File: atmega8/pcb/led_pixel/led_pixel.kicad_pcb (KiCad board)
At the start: 2 copper layers, 50 x 50 mm, 68 parts, among them IC1 ATMEGA8-AI, P1 USB_OTG, P10 CONN_01X04, P2 RESET, P3 CONN_01X03, P4 MOSI, P5 MISO, P6 SCK, P7 CONN_01X03, P8 5V, P9 GND, U1 MC78M05CDT, U2 PT4115, U3 PT4115, U4 SN75176, U5 PT4115, Y1 CRYSTAL

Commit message: layout in process... :|
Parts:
- removed the C7 at (162.0, 72.0)
- removed JP2: DMX_ADR_0, proz_jumper:solderjumper
- removed JP3: DMX_ADR_1, proz_jumper:solderjumper
- removed JP4: DMX_ADR_2, proz_jumper:solderjumper
- removed JP5: DMX_ADR_3, proz_jumper:solderjumper
- removed JP6: DMX_ADR_4, proz_jumper:solderjumper
- removed JP7: DMX_ADR_5, proz_jumper:solderjumper
- removed JP8: DMX_ADR_6, proz_jumper:solderjumper
- removed JP9: DMX_ADR_7, proz_jumper:solderjumper
- removed the P4 at (138.4, 82.5)
- removed the P5 at (141.0, 82.5)
- removed P6: SCK, Socket_Strips:Socket_Strip_Straight_1x01
- removed P8: 5V, Socket_Strips:Socket_Strip_Straight_1x01
- removed P9: GND, Socket_Strips:Socket_Strip_Straight_1x01
- added SW1: SW_DIP_x08, proz_switch:SW_DIP_x8_SMD_2.54, F.Cu at (168.3, 81.9)
- P2: value RESET -> ISP; footprint Socket_Strips:Socket_Strip_Straight_1x01 -> Connectors:IDC_Header_Straight_6pins
- moved P2 50.0 mm to (164.7, 41.7), turned to 270 degrees
- moved C10 14.4 mm to (137.3, 79.3)
- moved C3 13.2 mm to (148.0, 83.9), turned to 180 degrees
- moved P5 12.8 mm to (172.9, 111.8)
- moved C13 12.7 mm to (170.1, 104.0), turned to 270 degrees
- moved R16 12.7 mm to (168.8, 107.3)
- moved P3 12.4 mm to (172.9, 95.1)
- moved R15 11.6 mm to (168.8, 109.3), turned to 180 degrees
- moved C12 11.3 mm to (144.4, 111.8), turned to 180 degrees
- moved C14 11.3 mm to (132.7, 111.8), turned to 180 degrees
- moved C11 10.9 mm to (156.6, 111.8), turned to 180 degrees
- moved D7 9.96 mm to (164.2, 112.9), turned to 0 degrees
- moved R10 9.78 mm to (152.0, 110.8), turned to 270 degrees
- moved R12 9.71 mm to (140.3, 110.8), turned to 270 degrees
- moved R14 9.64 mm to (128.7, 110.8), turned to 270 degrees
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- renumbered C11 to C10, C12 to C11, C13 to C12, C14 to C13, C15 to C14, C8 to C7, C9 to C8, C10 to C9, D6 to D5, D5 to D6, P7 to P4, P10 to P5
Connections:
- net Net-(IC1-Pad28) renamed /DMX_5
- C4 pad 1: Net-(C4-Pad1) -> /RESET
- IC1 pad 17: Net-(IC1-Pad17) -> /SCK
- IC1 pad 2: Net-(IC1-Pad2) -> /DMX_6
- IC1 pad 23: Net-(IC1-Pad23) -> /DMX_0
- IC1 pad 24: Net-(IC1-Pad24) -> /DMX_1
- IC1 pad 25: Net-(IC1-Pad25) -> /DMX_2
- IC1 pad 26: Net-(IC1-Pad26) -> /DMX_3
- IC1 pad 27: Net-(IC1-Pad27) -> /DMX_4
- IC1 pad 29: Net-(C4-Pad1) -> /RESET
- IC1 pad 9: Net-(IC1-Pad9) -> /DMX_7
- P2 pad 1: Net-(C4-Pad1) -> /LED_B
- R4 pad 2: Net-(C4-Pad1) -> /RESET
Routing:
- net /DMX_5: track 36.4 -> 0.00 mm, vias 1 -> 0
- net +5V: track 38.4 -> 2.10 mm
- net /LED_R_A: track 3.60 -> 36.1 mm, vias 0 -> 4
- net /LED_B_A: track 0.00 -> 29.6 mm
- net Net-(IC1-Pad19): track 25.1 -> 0.00 mm, vias 1 -> 0
- net GND: track 45.4 -> 21.1 mm, vias 4 -> 1
- net /LED_B_K: track 0.00 -> 24.2 mm
- net /LED_G_A: track 0.00 -> 22.9 mm, vias 0 -> 2
- net /DMX_TX: track 21.3 -> 0.00 mm, vias 2 -> 0
- net /DMX_DIR: track 21.1 -> 0.00 mm, vias 2 -> 0
- net /LED_G_K: track 0.00 -> 18.8 mm
- net /LED_R: track 20.2 -> 2.68 mm, vias 2 -> 0
- net Net-(IC1-Pad9): track 17.3 -> 0.00 mm, vias 2 -> 0
- net /UDB_+: track 16.3 -> 0.00 mm
- net Net-(C4-Pad1): track 14.9 -> 0.00 mm, vias 2 -> 0
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
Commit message: finished first shot of the layout...
there are mounting holes missing...
...so what ;)
I hope to find a place for them this week...
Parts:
- added G***: LOGO, proz_logo:Shimatta_SolderMask, B.Cu at (136.0, 111.6)
- added REF**: MountingHole_3.2mm_M3_DIN965, Mounting_Holes:MountingHole_3.2mm_M3_DIN965, F.Cu at (111.9, 83.7)
- added REF**: KiCAD Logo, Symbols:Symbol_KiCAD-Logo_CopperAndSilkScreenTop, B.Cu at (166.5, 82.4)
- added REF***: OSHW-Logo2_7.3x6mm_Copper, Symbols:OSHW-Logo2_7.3x6mm_Copper, B.Cu at (169.1, 90.0)
- added REF***: WEEE-Logo_4.2x6mm_SilkScreen, Symbols:WEEE-Logo_4.2x6mm_SilkScreen, B.Cu at (167.8, 110.3)
- P2: moved to B.Cu
- moved P2 49.6 mm to (137.3, 83.0), turned to 0 degrees
- moved R16 2.59 mm to (166.3, 106.8)
- moved R15 2.54 mm to (166.3, 109.3)
- moved C13 0.80 mm to (169.3, 104.2)
- moved C5 0.77 mm to (155.8, 85.2)
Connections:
- P3 pad 2: Net-(IC1-Pad19) -> Net-(IC1-Pad22)
- P3 pad 3: Net-(IC1-Pad22) -> Net-(IC1-Pad19)
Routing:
- net GND: track 21.1 -> 202.9 mm, vias 1 -> 186
- net +5V: track 2.10 -> 158.3 mm, vias 0 -> 6
- net /LED_B: track 0.00 -> 46.7 mm, vias 0 -> 2
- net /DMX_DIR: track 0.00 -> 37.2 mm, vias 0 -> 2
- net /LED_G: track 0.00 -> 37.0 mm, vias 0 -> 3
- net /LED_R: track 2.68 -> 39.6 mm, vias 0 -> 4
- net Net-(IC1-Pad19): track 0.00 -> 33.1 mm
- net /DMX_5: track 0.00 -> 32.7 mm
- net /DMX_RX: track 0.00 -> 29.1 mm
- net VCC: track 19.5 -> 47.8 mm
- net Net-(IC1-Pad22): track 0.00 -> 28.2 mm
- net /RESET: track 0.00 -> 25.5 mm, vias 0 -> 3
- net /DMX_TX: track 0.00 -> 24.8 mm, vias 0 -> 2
- net /Bootloader: track 0.00 -> 19.3 mm
- net /DMX_6: track 0.00 -> 16.6 mm
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- added copper zone on B.Cu, net GND
- added copper zone on F.Cu, net GND
- added copper zone on F.Cu, net VCC

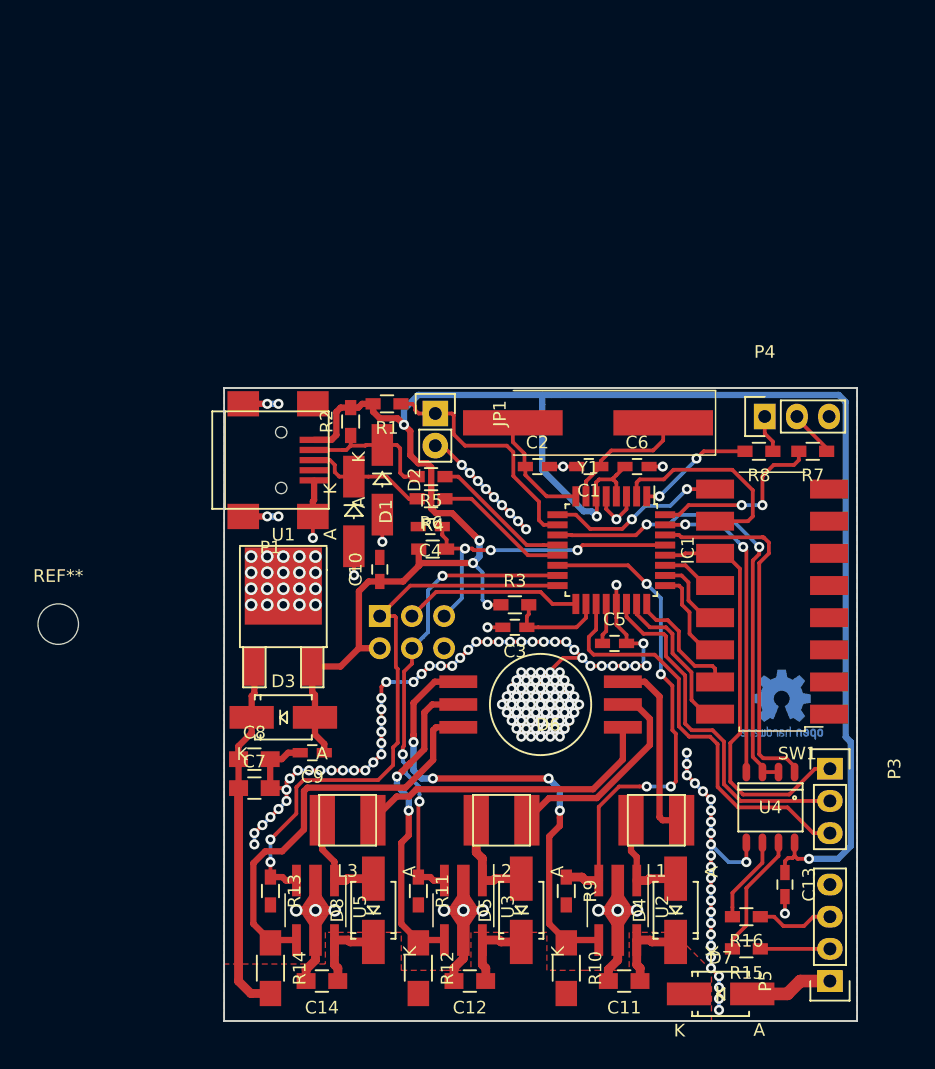
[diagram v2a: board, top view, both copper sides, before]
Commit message: finished rought layout with mounting holes and needle debug adaptor...
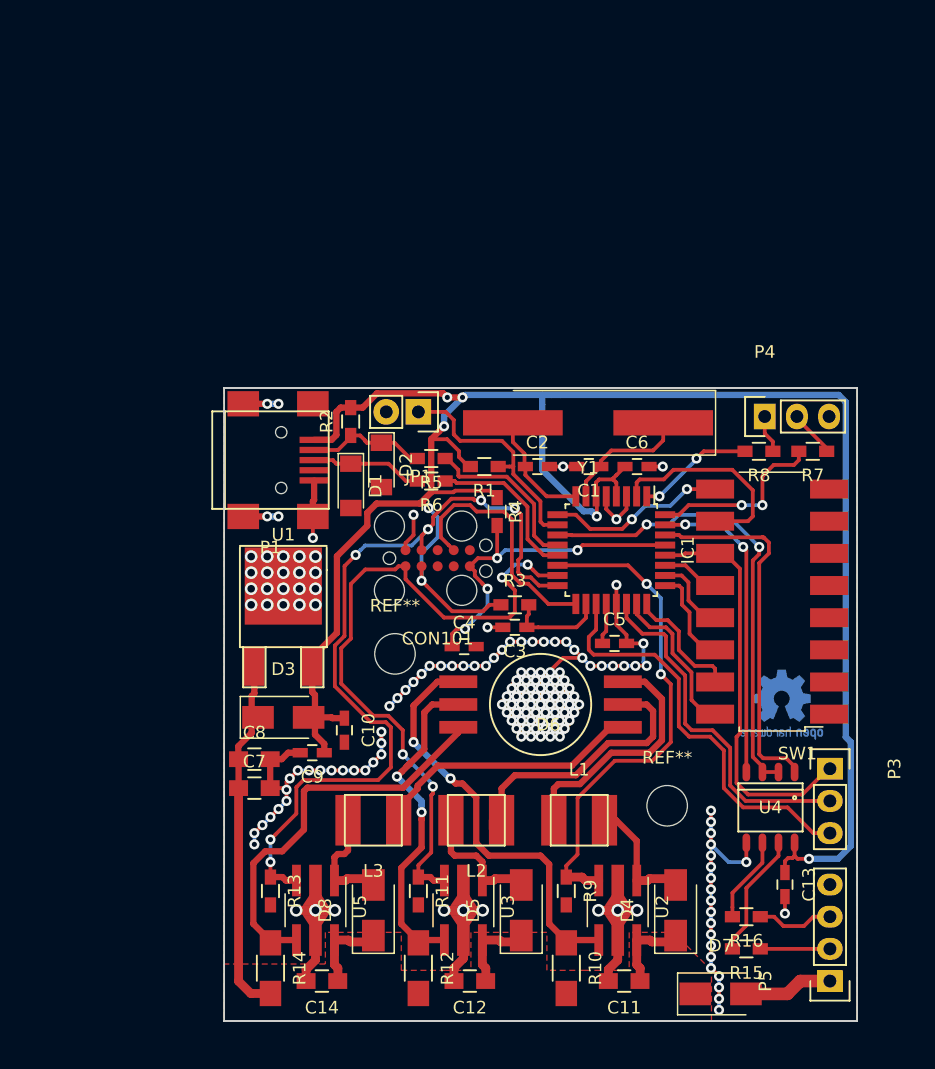
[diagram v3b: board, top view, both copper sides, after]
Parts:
- removed P2: ISP, Connectors:IDC_Header_Straight_6pins
- added CON101: 10PIN_ISP_AVR, proz_connectors:TC2050-IDC, F.Cu at (141.9, 78.4)
- added REF**: MountingHole_3.2mm_M3_DIN965, Mounting_Holes:MountingHole_3.2mm_M3_DIN965, F.Cu at (138.5, 86.0)
- D1, D2: footprint Diodes_SMD:MiniMELF_Handsoldering -> Diodes_SMD:D_MiniMELF_Standard
- D3, D4, D5, D7, D8: footprint Diodes_SMD:SMA_Handsoldering -> Diodes_SMD:D_SMA_Standard
- moved REF** 50.2 mm to (160.0, 98.0)
- moved C10 13.0 mm to (134.5, 92.0), turned to 270 degrees
- moved C4 9.85 mm to (144.0, 85.4), turned to 0 degrees
- moved R1 9.14 mm to (145.6, 71.2)
- moved L1 6.10 mm to (153.0, 99.1), turned to 0 degrees
- moved R4 5.89 mm to (146.6, 74.8), turned to 270 degrees
- moved D1 2.04 mm to (135.0, 72.7)
- moved L3 2.03 mm to (136.8, 99.1)
- moved L2 2.00 mm to (144.9, 99.1)
- moved R5 1.43 mm to (141.4, 70.6)
- moved R6 1.40 mm to (141.4, 72.3)
- moved JP1 1.34 mm to (140.3, 66.9), turned to 180 degrees
- moved D2 1.18 mm to (137.4, 71.1)
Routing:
- net GND: track 202.9 -> 182.7 mm, vias 186 -> 169
- net /LED_B: track 46.7 -> 64.0 mm, vias 2 -> 6
- net /LED_G: track 37.0 -> 54.1 mm, vias 3 -> 4
- net +5V: track 158.3 -> 171.4 mm, vias 6 -> 7
- net /SCK: track 14.1 -> 19.8 mm
- net /LED_R_K: track 14.8 -> 19.5 mm
- net /LED_G_K: track 16.8 -> 21.5 mm
- net /LED_R_A: track 37.4 -> 33.5 mm, vias 4 -> 2
- net /LED_B_K: track 24.3 -> 21.5 mm
- net /USB_-: track 11.1 -> 13.5 mm
- net /UDB_+: track 10.7 -> 12.8 mm
- net Net-(D5-Pad2): track 8.10 -> 9.92 mm
- net Net-(D2-Pad1): track 11.3 -> 9.50 mm
- net /RESET: track 25.5 -> 27.2 mm, vias 3 -> 4
- net Net-(D4-Pad2): track 8.08 -> 9.49 mm
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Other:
- net class Default: trace_width 0.25 -> 0.3
- rule trace_min: 0.2 -> 0.3

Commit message: finished... I hope...
replaced the ref descriptors...
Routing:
- net GND: track 182.7 -> 190.4 mm, vias 169 -> 176
- net /LED_G: track 54.1 -> 55.2 mm
- net /LED_G_A: track 26.6 -> 27.5 mm
- net /DMX_2: track 7.79 -> 8.51 mm
- net /DMX_3: track 6.17 -> 6.82 mm
- net Net-(IC1-Pad22): track 28.1 -> 27.5 mm

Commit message: did some final fixes...
created doku package and gerber files...
ready for chinese PCB production ;)
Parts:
- moved R2 0.25 mm to (135.0, 67.9)
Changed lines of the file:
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@@
     (thickness 1.6)
     (drawings 4)
-    (tracks 1031)
+    (tracks 1033)
     (zones 0)
     (modules 61)
@@
   )
   (setup
-    (last_trace_width 0.3)
+    (last_trace_width 0.5)
     (user_trace_width 0.3)
     (user_trace_width 0.5)
@@
     (visible_elements 7FFFFFFF)
     (pcbplotparams
-      (layerselection 0x00030_ffffffff)
-      (usegerberextensions false)
+      (layerselection 0x010fc_ffffffff)
+      (usegerberextensions true)
       (excludeedgelayer true)
       (linewidth 0.100000)
@@
       (plotinvisibletext false)
       (padsonsilk false)
-      (subtractmaskfromsilk false)
+      (subtractmaskfromsilk true)
       (outputformat 1)
       (mirror false)
-      (drillshape 1)
+      (drillshape 0)
       (scaleselection 1)
-      (outputdirectory ""))
+      (outputdirectory gerber))
   )
   (net 0 "")
@@
     (tags "resistor 0603")
     (attr smd)
-    (fp_text reference R1 (at 0 -1.9 180) (layer F.SilkS)
+    (fp_text reference R1 (at 1.143 -1.524 180) (layer F.SilkS)
       (effects (font (size 1 1) (thickness 0.15)))
     )
@@
   )
   (module Resistors_SMD:R_0603_HandSoldering (layer F.Cu)
-    (at 135 67.648 90)
+    (at 135.014 67.902 90)
     (descr "Resistor SMD 0603, hand soldering")
     (tags "resistor 0603")
     (attr smd)
-    (fp_text reference R2 (at 1.778 -1.256 90) (layer F.SilkS)
-      (effects (font (size 1 1) (thickness 0.15)))
+    (fp_text reference R2 (at 2.286 0 180) (layer F.SilkS)
+      (effects (font (size 0.7 0.7) (thickness 0.1)))
     )
     (fp_text value 2k2 (at 0 1.9 90) (layer F.Fab)
@@
     (tags "resistor 0603")
     (attr smd)
-    (fp_text reference R4 (at 0 -1.45 270) (layer F.SilkS)
+    (fp_text reference R4 (at 1.27 -1.45 270) (layer F.SilkS)
       (effects (font (size 1 1) (thickness 0.15)))
     )
@@
   (segment (start 132.01426 76.84026) (end 132.0168 76.8428) (width 0.3) (layer F.Cu) (net 1))
   (via (at 132.0168 76.8428) (size 0.8) (drill 0.4) (layers F.Cu B.Cu) (net 1))
+  (segment (start 142.634 65.743) (end 142.310999 65.419999) (width 0.5) (layer F.Cu) (net 2))
+  (segment (start 142.310999 65.419999) (end 136.480001 65.419999) (width 0.5) (layer F.Cu) (net 2))
+  (segment (start 136.480001 65.419999) (end 136.03 65.87) (width 0.5) (layer F.Cu) (net 2))
+  (segment (start 136.03 65.87) (end 136.03 66.736) (width 0.5) (layer F.Cu) (net 2))
+  (segment (start 136.03 66.736) (end 135.964 66.802) (width 0.5) (layer F.Cu) (net 2))
+  (segment (start 135.964 66.802) (end 135.014 66.802) (width 0.5) (layer F.Cu) (net 2))
+  (segment (start 132.11332 69.0958) (end 133.49 69.0958) (width 0.5) (layer F.Cu) (net 2))
+  (segment (start 133.49 69.0958) (end 133.871 68.7148) (width 0.5) (layer F.Cu) (net 2))
+  (segment (start 133.871 67.013) (end 134.082 66.802) (width 0.5) (layer F.Cu) (net 2))
+  (segment (start 133.871 68.7148) (end 133.871 67.013) (width 0.5) (layer F.Cu) (net 2))
+  (segment (start 134.082 66.802) (end 135.014 66.802) (width 0.5) (layer F.Cu) (net 2))
   (segment (start 131.966 86.285336) (end 131.966 86.995) (width 0.5) (layer F.Cu) (net 2))
   (segment (start 133.532978 78.666018) (end 133.532978 84.718358) (width 0.5) (layer F.Cu) (net 2))
@@
   (via (at 143.834999 65.743) (size 0.8) (drill 0.4) (layers F.Cu B.Cu) (net 2))
   (segment (start 143.834999 65.743) (end 142.38 67.197999) (width 0.5) (layer B.Cu) (net 2))
-  (segment (start 142.310999 65.419999) (end 142.634 65.743) (width 0.5) (layer F.Cu) (net 2))
   (via (at 142.634 65.743) (size 0.8) (drill 0.4) (layers F.Cu B.Cu) (net 2))
-  (segment (start 142.183999 65.419999) (end 142.310999 65.419999) (width 0.5) (layer F.Cu) (net 2))
   (segment (start 144.455 71.204) (end 144.305 71.204) (width 0.3) (layer F.Cu) (net 2) (status 30))
   (segment (start 144.305 71.204) (end 143.555 70.454) (width 0.3) (layer F.Cu) (net 2) (status 10))
@@
   (via (at 142.38 68.029006) (size 0.8) (drill 0.4) (layers F.Cu B.Cu) (net 2))
   (segment (start 144.031 65.546999) (end 150.127 65.546999) (width 0.5) (layer B.Cu) (net 2))
-  (segment (start 135 66.548) (end 135.95 66.548) (width 0.5) (layer F.Cu) (net 2) (status 10))
-  (segment (start 137.078001 65.419999) (end 142.183999 65.419999) (width 0.5) (layer F.Cu) (net 2))
-  (segment (start 135.95 66.548) (end 137.078001 65.419999) (width 0.5) (layer F.Cu) (net 2))
   (segment (start 151.581999 65.546999) (end 173.552999 65.546999) (width 0.5) (layer B.Cu) (net 2))
   (segment (start 150.127 65.546999) (end 150.889 65.546999) (width 0.5) (layer B.Cu) (net 2))
@@
   (segment (start 153.410001 74.741001) (end 150.127 71.458) (width 0.5) (layer B.Cu) (net 2))
   (segment (start 150.889 65.546999) (end 151.581999 65.546999) (width 0.5) (layer B.Cu) (net 2))
-  (segment (start 135 66.548) (end 134.209 66.548) (width 0.5) (layer F.Cu) (net 2) (status 10))
-  (segment (start 134.209 66.548) (end 133.871 66.886) (width 0.5) (layer F.Cu) (net 2))
-  (segment (start 133.49 69.0958) (end 132.11332 69.0958) (width 0.5) (layer F.Cu) (net 2) (status 20))
-  (segment (start 133.871 66.886) (end 133.871 68.7148) (width 0.5) (layer F.Cu) (net 2))
-  (segment (start 133.871 68.7148) (end 133.49 69.0958) (width 0.5) (layer F.Cu) (net 2))
   (segment (start 173.495 102.192) (end 171.209 102.192) (width 0.5) (layer B.Cu) (net 2))
   (segment (start 173.552999 65.546999) (end 174.10361 66.09761) (width 0.5) (layer B.Cu) (net 2))
@@
   (segment (start 133.864 70.978) (end 135.014 70.978) (width 0.3) (layer F.Cu) (net 23) (status 20))
   (segment (start 132.11332 70.696) (end 133.617 70.696) (width 0.3) (layer F.Cu) (net 23) (status 10))
+  (segment (start 137.427 69.327) (end 136.277 69.327) (width 0.3) (layer F.Cu) (net 24))
+  (segment (start 136.277 69.327) (end 135.952 69.002) (width 0.3) (layer F.Cu) (net 24))
+  (segment (start 135.952 69.002) (end 135.014 69.002) (width 0.3) (layer F.Cu) (net 24))
+  (segment (start 132.11332 69.8959) (end 133.2741 69.8959) (width 0.3) (layer F.Cu) (net 24))
+  (segment (start 133.2741 69.8959) (end 133.2802 69.902) (width 0.3) (layer F.Cu) (net 24))
+  (segment (start 133.2802 69.902) (end 134.264 69.902) (width 0.3) (layer F.Cu) (net 24))
+  (segment (start 134.264 69.902) (end 135.014 69.152) (width 0.3) (layer F.Cu) (net 24))
+  (segment (start 135.014 69.152) (end 135.014 69.002) (width 0.3) (layer F.Cu) (net 24))
   (segment (start 137.427 69.327) (end 138.471 69.327) (width 0.3) (layer F.Cu) (net 24) (status 10))
   (segment (start 138.471 69.327) (end 139.713 70.569) (width 0.3) (layer F.Cu) (net 24) (status 20))
   (segment (start 139.713 70.569) (end 140.264 70.569) (width 0.3) (layer F.Cu) (net 24) (status 30))
-  (segment (start 136.157 69.155) (end 136.157 69.207) (width 0.3) (layer F.Cu) (net 24))
-  (segment (start 136.157 69.207) (end 136.277 69.327) (width 0.3) (layer F.Cu) (net 24))
-  (segment (start 136.277 69.327) (end 137.427 69.327) (width 0.3) (layer F.Cu) (net 24) (status 20))
-  (segment (start 135 68.748) (end 135.75 68.748) (width 0.3) (layer F.Cu) (net 24) (status 10))
-  (segment (start 135.75 68.748) (end 136.157 69.155) (width 0.3) (layer F.Cu) (net 24))
-  (segment (start 132.11332 69.8959) (end 134.0021 69.8959) (width 0.3) (layer F.Cu) (net 24) (status 10))
-  (segment (start 134.0021 69.8959) (end 135 68.898) (width 0.3) (layer F.Cu) (net 24) (status 20))
   (segment (start 135 68.898) (end 135 68.748) (width 0.3) (layer F.Cu) (net 24) (status 30))
   (segment (start 155.048 99.144) (end 155.969 99.144) (width 0.5) (layer F.Cu) (net 25))
